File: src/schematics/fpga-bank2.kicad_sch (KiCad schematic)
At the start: 1 part

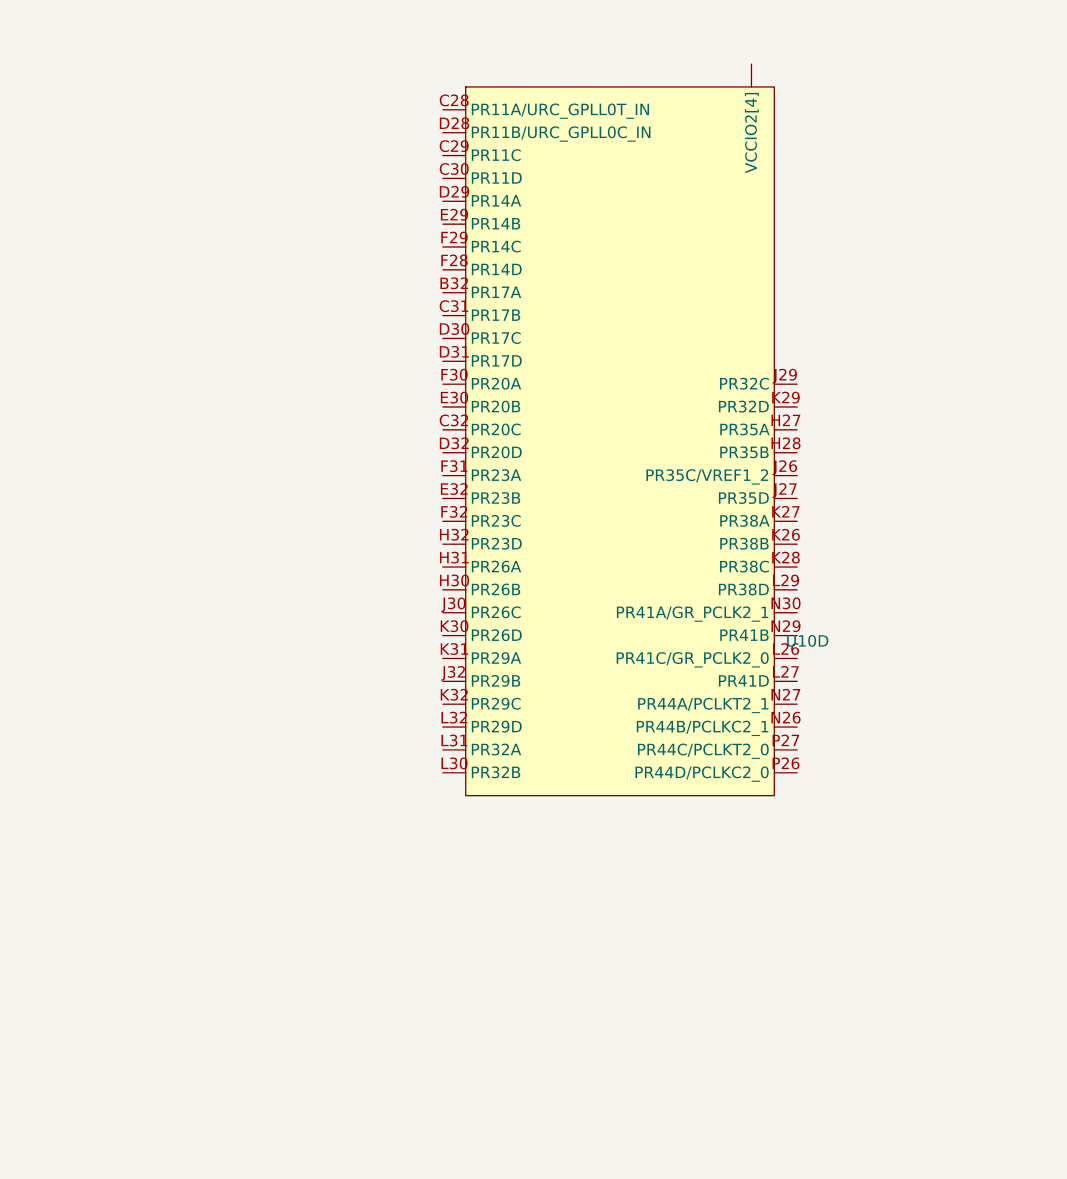
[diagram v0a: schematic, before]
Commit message: Draft connections between the FPGA and the memories
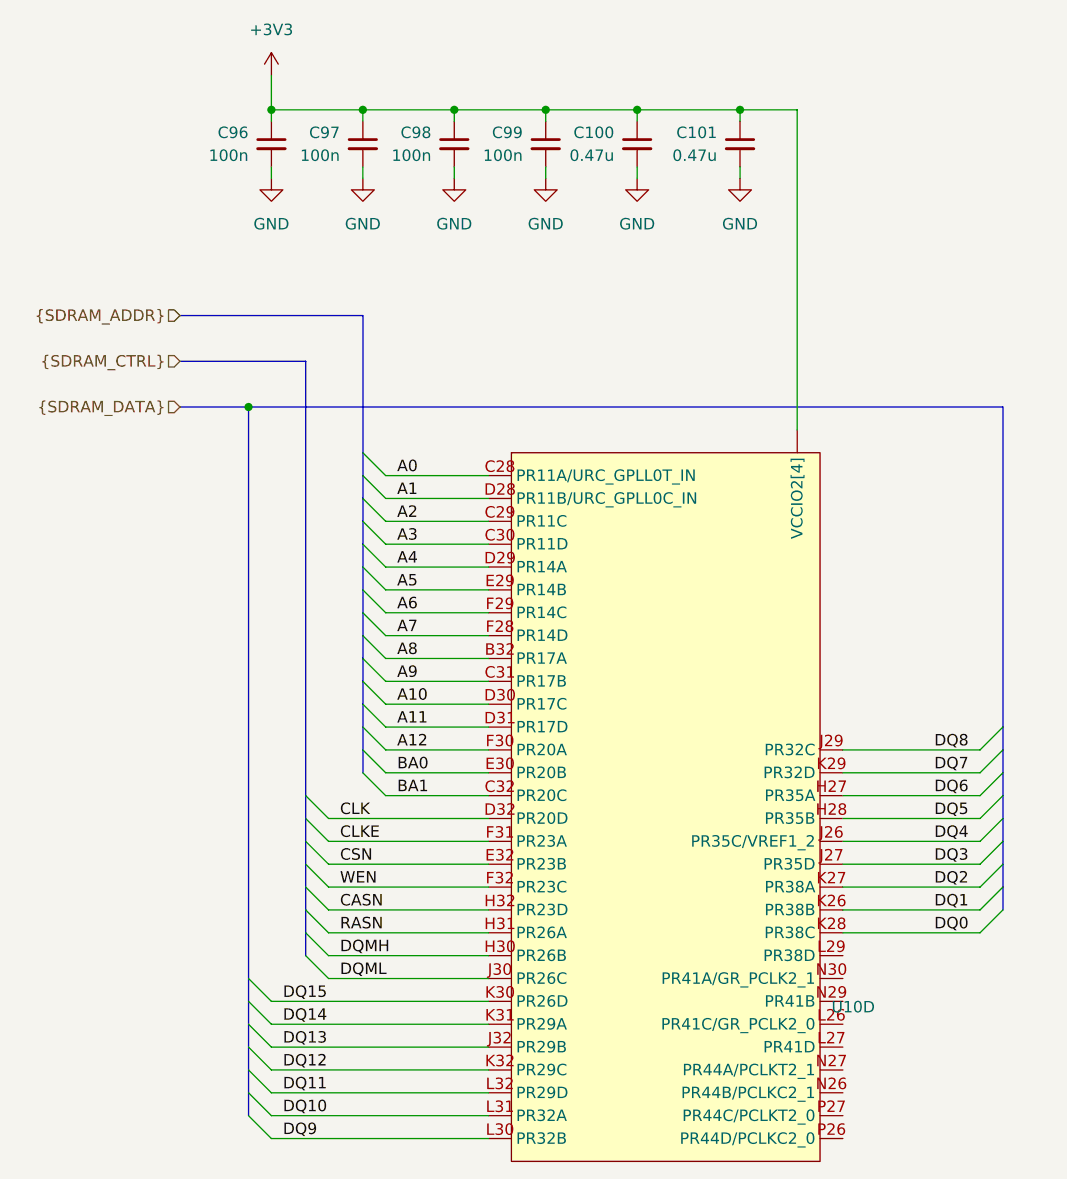
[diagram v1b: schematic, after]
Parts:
- added C100, C101: 0.47u, symbol Device:C_Small
- added C96, C97, C98, C99: 100n, symbol Device:C_Small
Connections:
- net A8: now reaches U10.B32 (PR17A)
- net A0: now reaches U10.C28 (PR11A/URC_GPLL0T_IN)
- net A2: now reaches U10.C29 (PR11C)
- net A3: now reaches U10.C30 (PR11D)
- net A9: now reaches U10.C31 (PR17B)
- net BA1: now reaches U10.C32 (PR20C)
- net A1: now reaches U10.D28 (PR11B/URC_GPLL0C_IN)
- net A4: now reaches U10.D29 (PR14A)
- net A10: now reaches U10.D30 (PR17C)
- net A11: now reaches U10.D31 (PR17D)
- net CLK: now reaches U10.D32 (PR20D)
- net A5: now reaches U10.E29 (PR14B)
- net BA0: now reaches U10.E30 (PR20B)
- net CSN: now reaches U10.E32 (PR23B)
- net A7: now reaches U10.F28 (PR14D)
- net A6: now reaches U10.F29 (PR14C)
- net A12: now reaches U10.F30 (PR20A)
- net CLKE: now reaches U10.F31 (PR23A)
- net WEN: now reaches U10.F32 (PR23C)
- net DQ6: now reaches U10.H27 (PR35A)
- net DQ5: now reaches U10.H28 (PR35B)
- net DQMH: now reaches U10.H30 (PR26B)
- net RASN: now reaches U10.H31 (PR26A)
- net CASN: now reaches U10.H32 (PR23D)
- net DQ4: now reaches U10.J26 (PR35C/VREF1_2)
- net DQ3: now reaches U10.J27 (PR35D)
- net DQ8: now reaches U10.J29 (PR32C)
- net DQML: now reaches U10.J30 (PR26C)
- net DQ13: now reaches U10.J32 (PR29B)
- net DQ1: now reaches U10.K26 (PR38B)
- net DQ2: now reaches U10.K27 (PR38A)
- net DQ0: now reaches U10.K28 (PR38C)
- net DQ7: now reaches U10.K29 (PR32D)
- net DQ15: now reaches U10.K30 (PR26D)
- net DQ14: now reaches U10.K31 (PR29A)
- net DQ12: now reaches U10.K32 (PR29C)
- net DQ9: now reaches U10.L30 (PR32B)
- net DQ10: now reaches U10.L31 (PR32A)
- net DQ11: now reaches U10.L32 (PR29D)
- net VCCIO2 renamed +3V3
- net +3V3: now also C100.1, C101.1, C96.1, C97.1, C98.1, C99.1
- new net GND: C100.2, C101.2, C96.2, C97.2, C98.2, C99.2
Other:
- moved on the sheet: U10D

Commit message: Adds draft of IO connector schematic connections to FPGA
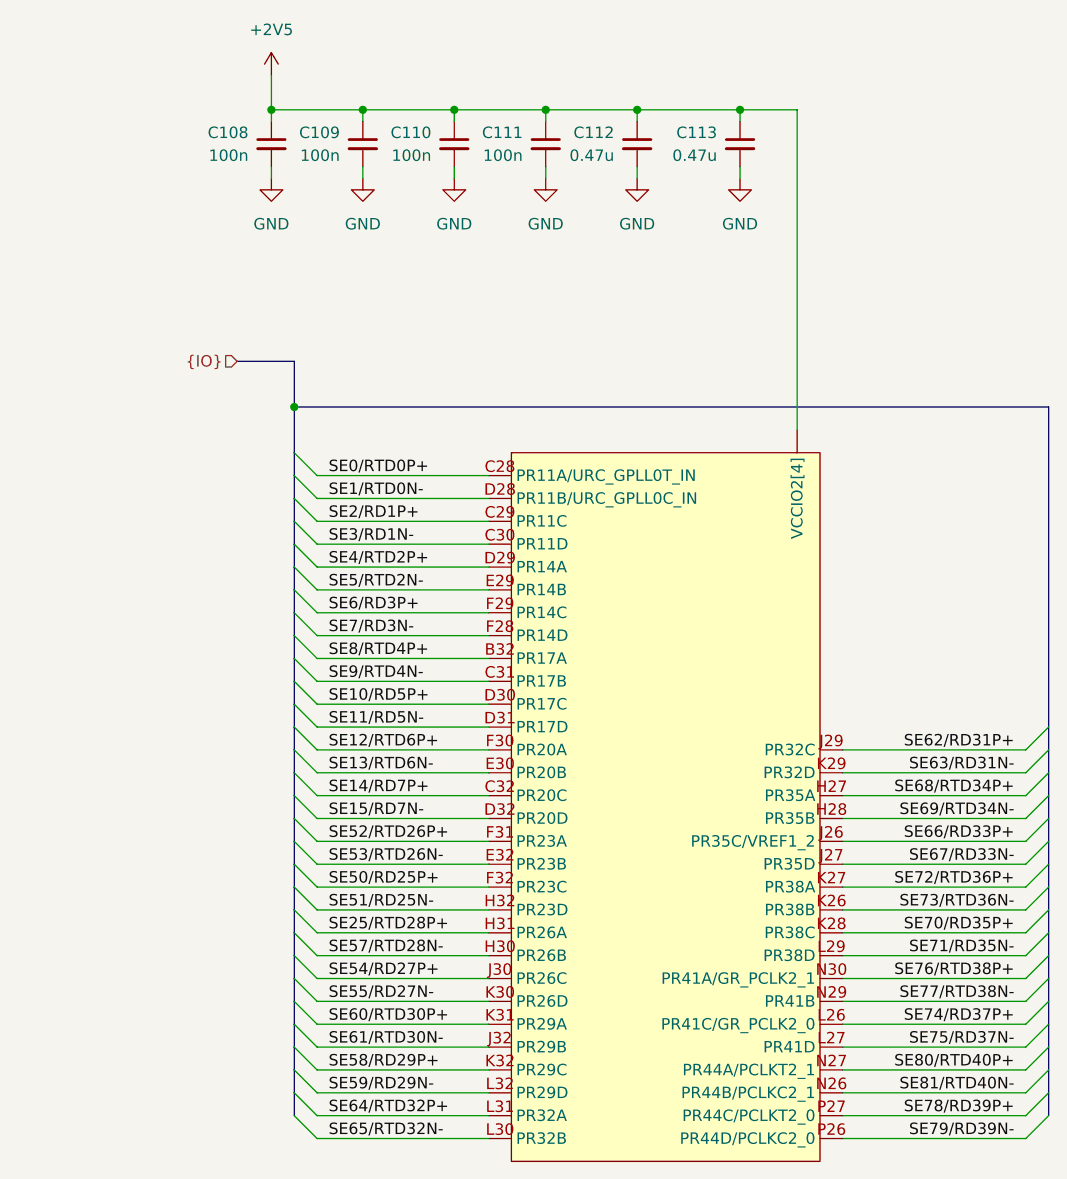
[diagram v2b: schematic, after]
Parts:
- removed C100, C101: 0.47u, symbol Device:C_Small
- removed C96, C97, C98, C99: 100n, symbol Device:C_Small
- added C108, C109, C110, C111: 100n, symbol Device:C_Small
- added C112, C113: 0.47u, symbol Device:C_Small
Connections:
- net GND: now also C108.2, C109.2, C110.2, C111.2, C112.2, C113.2
- net SE74/RD37P+: now reaches U10.L26 (PR41C/GR_PCLK2_0)
- net SE75/RD37N-: now reaches U10.L27 (PR41D)
- net SE71/RD35N-: now reaches U10.L29 (PR38D)
- net SE81/RTD40N-: now reaches U10.N26 (PR44B/PCLKC2_1)
- net SE80/RTD40P+: now reaches U10.N27 (PR44A/PCLKT2_1)
- net SE77/RTD38N-: now reaches U10.N29 (PR41B)
- net SE76/RTD38P+: now reaches U10.N30 (PR41A/GR_PCLK2_1)
- net SE79/RD39N-: now reaches U10.P26 (PR44D/PCLKC2_0)
- net SE78/RD39P+: now reaches U10.P27 (PR44C/PCLKT2_0)
- net +3V3 renamed +2V5
- net +2V5: now also C108.1, C109.1, C110.1, C111.1, C112.1, C113.1
- net A0 renamed SE0/RTD0P+
- net A1 renamed SE1/RTD0N-
- net A10 renamed SE10/RD5P+
- net A11 renamed SE11/RD5N-
- net A12 renamed SE12/RTD6P+
- net A2 renamed SE2/RD1P+
- net A3 renamed SE3/RD1N-
- net A4 renamed SE4/RTD2P+
- net A5 renamed SE5/RTD2N-
- net A6 renamed SE6/RD3P+
- net A7 renamed SE7/RD3N-
- net A8 renamed SE8/RTD4P+
- net A9 renamed SE9/RTD4N-
- net BA0 renamed SE13/RTD6N-
- net BA1 renamed SE14/RD7P+
- net CASN renamed SE51/RD25N-
- net CLK renamed SE15/RD7N-
- net CLKE renamed SE52/RTD26P+
- net CSN renamed SE53/RTD26N-
- net DQ0 renamed SE70/RD35P+
- net DQ1 renamed SE73/RTD36N-
- net DQ10 renamed SE64/RTD32P+
- net DQ11 renamed SE59/RD29N-
- net DQ12 renamed SE58/RD29P+
- net DQ13 renamed SE61/RTD30N-
- net DQ14 renamed SE60/RTD30P+
- net DQ15 renamed SE55/RD27N-
- net DQ2 renamed SE72/RTD36P+
- net DQ3 renamed SE67/RD33N-
- net DQ4 renamed SE66/RD33P+
- net DQ5 renamed SE69/RTD34N-
- net DQ6 renamed SE68/RTD34P+
- net DQ7 renamed SE63/RD31N-
- net DQ8 renamed SE62/RD31P+
- net DQ9 renamed SE65/RTD32N-
- net DQMH renamed SE57/RTD28N-
- net DQML renamed SE54/RD27P+
- net RASN renamed SE25/RTD28P+
- net WEN renamed SE50/RD25P+

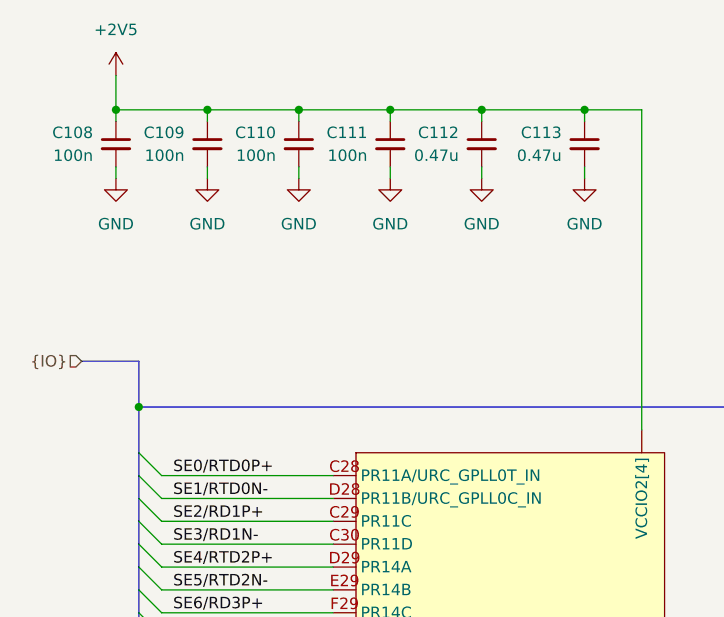
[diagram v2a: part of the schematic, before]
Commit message: Adds the clock oscillator
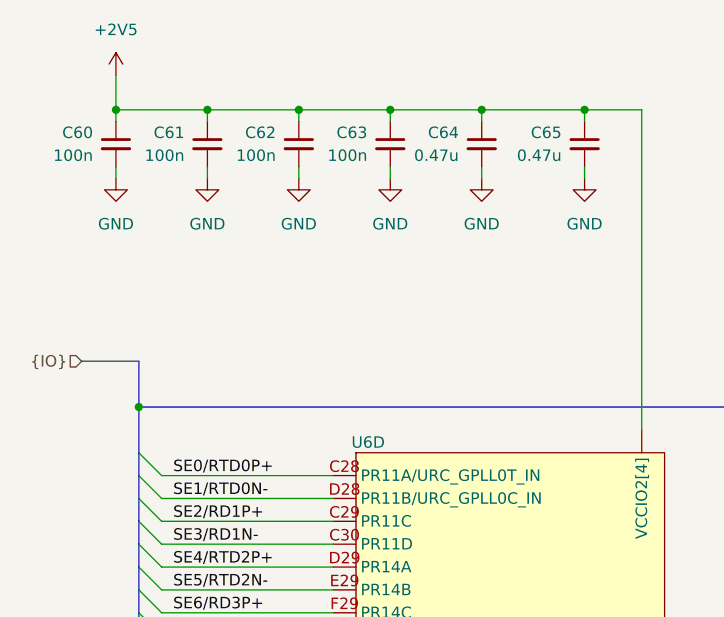
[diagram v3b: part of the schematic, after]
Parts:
- removed U10: ~, symbol ECAP5-BSOM:LFE5U-85F-*BG756*
- added U6: ~, symbol ECAP5-BSOM:LFE5U-85F-*BG756*
- renumbered C108 to C60, C109 to C61, C110 to C62, C111 to C63, C112 to C64, C113 to C65
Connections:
- net +2V5: now also U6. (VCCIO2[4]), U6.M23 (VCCIO2), U6.P23 (VCCIO2), U6.R23 (VCCIO2), U6.T23 (VCCIO2)
- net SE0/RTD0P+: now also U6.C28 (PR11A/URC_GPLL0T_IN)
- net SE10/RD5P+: now also U6.D30 (PR17C)
- net SE11/RD5N-: now also U6.D31 (PR17D)
- net SE12/RTD6P+: now also U6.F30 (PR20A)
- net SE13/RTD6N-: now also U6.E30 (PR20B)
- net SE14/RD7P+: now also U6.C32 (PR20C)
- net SE15/RD7N-: now also U6.D32 (PR20D)
- net SE1/RTD0N-: now also U6.D28 (PR11B/URC_GPLL0C_IN)
- net SE25/RTD28P+: now also U6.H31 (PR26A)
- net SE2/RD1P+: now also U6.C29 (PR11C)
- net SE3/RD1N-: now also U6.C30 (PR11D)
- net SE4/RTD2P+: now also U6.D29 (PR14A)
- net SE50/RD25P+: now also U6.F32 (PR23C)
- net SE51/RD25N-: now also U6.H32 (PR23D)
- net SE52/RTD26P+: now also U6.F31 (PR23A)
- net SE53/RTD26N-: now also U6.E32 (PR23B)
- net SE54/RD27P+: now also U6.J30 (PR26C)
- net SE55/RD27N-: now also U6.K30 (PR26D)
- net SE57/RTD28N-: now also U6.H30 (PR26B)
- net SE58/RD29P+: now also U6.K32 (PR29C)
- net SE59/RD29N-: now also U6.L32 (PR29D)
- net SE5/RTD2N-: now also U6.E29 (PR14B)
- net SE60/RTD30P+: now also U6.K31 (PR29A)
- net SE61/RTD30N-: now also U6.J32 (PR29B)
- net SE62/RD31P+: now also U6.J29 (PR32C)
- net SE63/RD31N-: now also U6.K29 (PR32D)
- net SE64/RTD32P+: now also U6.L31 (PR32A)
- net SE65/RTD32N-: now also U6.L30 (PR32B)
- net SE66/RD33P+: now also U6.J26 (PR35C/VREF1_2)
- net SE67/RD33N-: now also U6.J27 (PR35D)
- net SE68/RTD34P+: now also U6.H27 (PR35A)
- net SE69/RTD34N-: now also U6.H28 (PR35B)
- net SE6/RD3P+: now also U6.F29 (PR14C)
- net SE70/RD35P+: now also U6.K28 (PR38C)
- net SE71/RD35N-: now also U6.L29 (PR38D)
- net SE72/RTD36P+: now also U6.K27 (PR38A)
- net SE73/RTD36N-: now also U6.K26 (PR38B)
- net SE74/RD37P+: now also U6.L26 (PR41C/GR_PCLK2_0)
- net SE75/RD37N-: now also U6.L27 (PR41D)
- net SE76/RTD38P+: now also U6.N30 (PR41A/GR_PCLK2_1)
- net SE77/RTD38N-: now also U6.N29 (PR41B)
- net SE78/RD39P+: now also U6.P27 (PR44C/PCLKT2_0)
- net SE79/RD39N-: now also U6.P26 (PR44D/PCLKC2_0)
- net SE7/RD3N-: now also U6.F28 (PR14D)
- net SE80/RTD40P+: now also U6.N27 (PR44A/PCLKT2_1)
- net SE81/RTD40N-: now also U6.N26 (PR44B/PCLKC2_1)
- net SE8/RTD4P+: now also U6.B32 (PR17A)
- net SE9/RTD4N-: now also U6.C31 (PR17B)

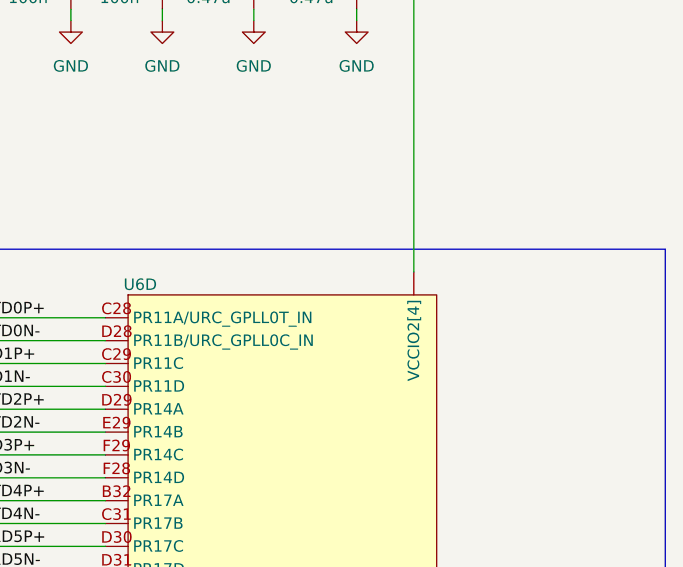
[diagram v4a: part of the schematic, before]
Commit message: Fix some ERC issues
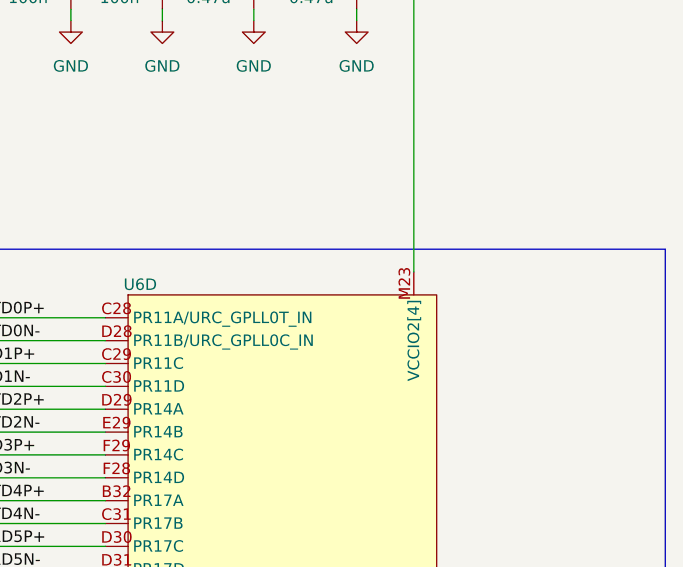
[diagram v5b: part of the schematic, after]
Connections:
- net +2V5: no longer U6. (VCCIO2[4])
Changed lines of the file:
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@@
 		(pin "Y31"
 		)
-		(pin ""
-		)
 		(pin "A10"
 		)
@@
 		(pin "Y32"
 		)
-		(pin ""
-		)
 		(pin "AB23"
 		)
@@
 		(pin "K16"
 		)
-		(pin ""
-		)
 		(pin "A18"
 		)
@@
 		(pin "K21"
 		)
-		(pin ""
-		)
 		(pin "B32"
 		)
@@
 		(pin "T23"
 		)
-		(pin ""
-		)
 		(pin "AA23"
 		)
@@
 		(pin "AM31"
 		)
-		(pin ""
-		)
 		(pin "AA10"
 		)
@@
 		(pin "Y7"
 		)
-		(pin ""
-		)
 		(pin "B1"
 		)
@@
 		(pin "T10"
 		)
-		(pin ""
-		)
 		(pin "AB10"
 		)
@@
 		(pin "M14"
 		)
-		(pin ""
-		)
 		(pin "AH12"
 		)
@@
 		(pin "V19"
 		)
-		(pin ""
-		)
 		(pin "AC11"
 		)
@@
 		(pin "AA11"
 		)
-		(pin ""
-		)
 		(instances

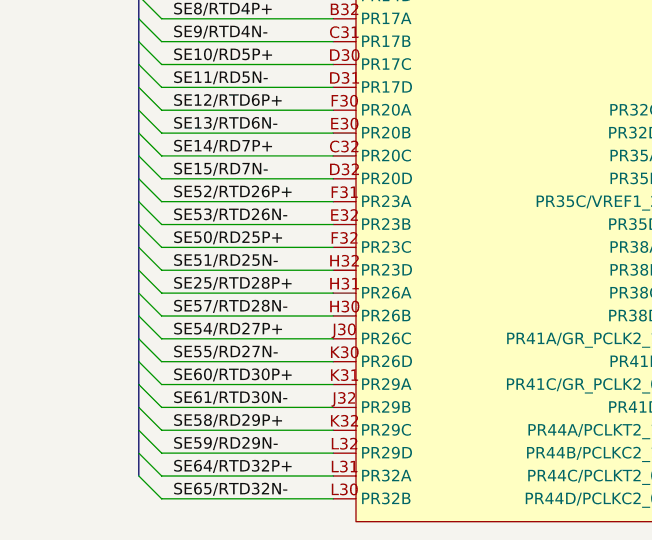
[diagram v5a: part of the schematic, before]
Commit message: Fixes bus aliases
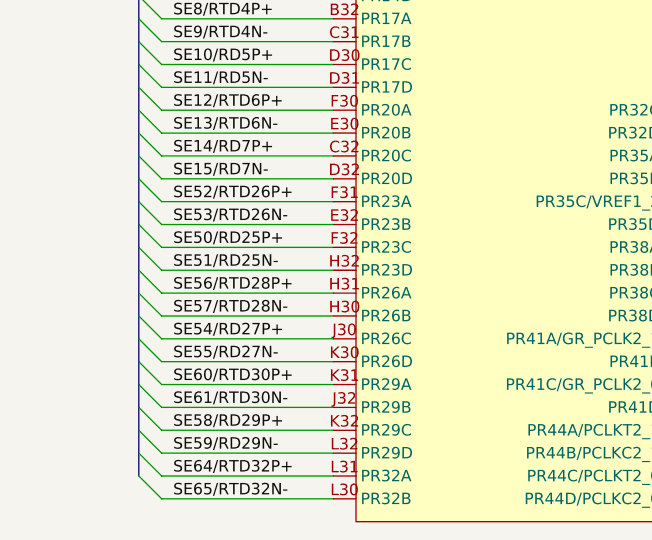
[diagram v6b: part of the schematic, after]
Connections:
- net SE25/RTD28P+ renamed SE56/RTD28P+
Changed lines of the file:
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@@
 		)
 	)
-	(label "SE25{slash}RTD28P+"
+	(label "SE56{slash}RTD28P+"
 		(at 121.92 125.73 0)
 		(fields_autoplaced yes)
@@
 		(pin "AB32"
 		)
-		(pin "AB32"
+		(pin "AB31"
 		)
 		(pin "AC26"
